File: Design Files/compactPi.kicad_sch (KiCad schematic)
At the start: 8 parts, among them J15 USB_C_Receptacle_USB2.0, U22 WE-TVS-82400102, U23 WE-TVS-82400102

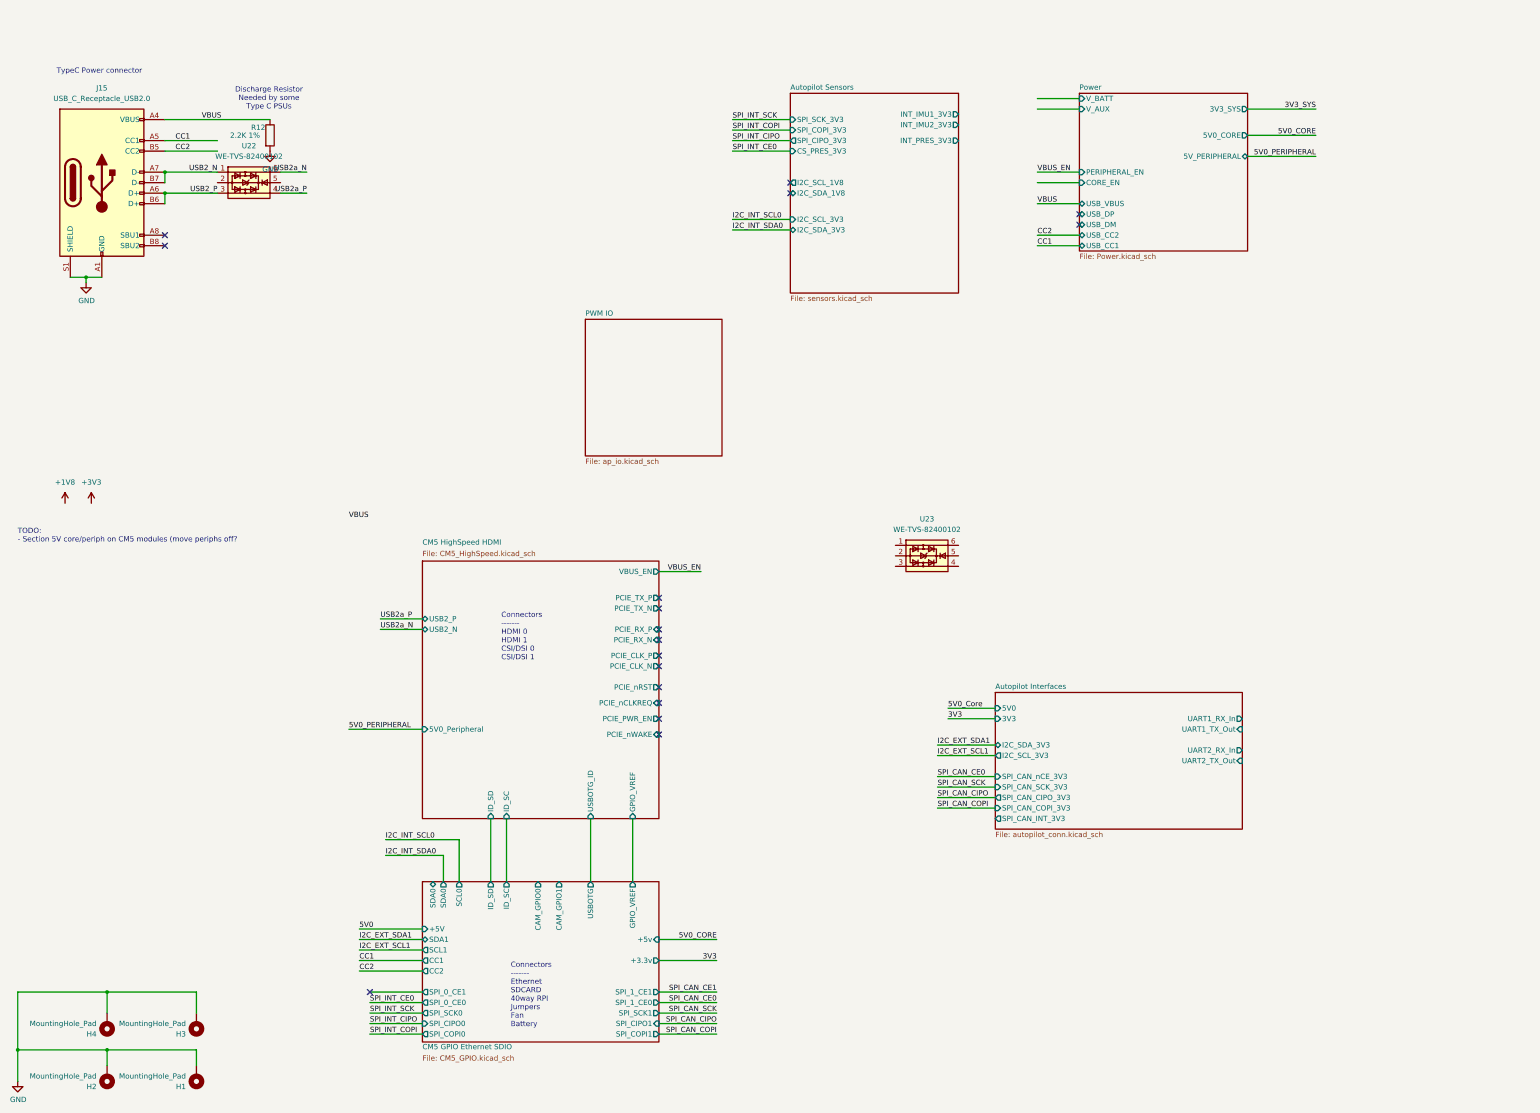
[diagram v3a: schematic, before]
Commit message: Fixed power & GPIO nets
Added PWM I2C Bus
Replaced global power labels on the sensor page with hierarchical pins & page labels
Cleaned up CM5 GPIO block sheet
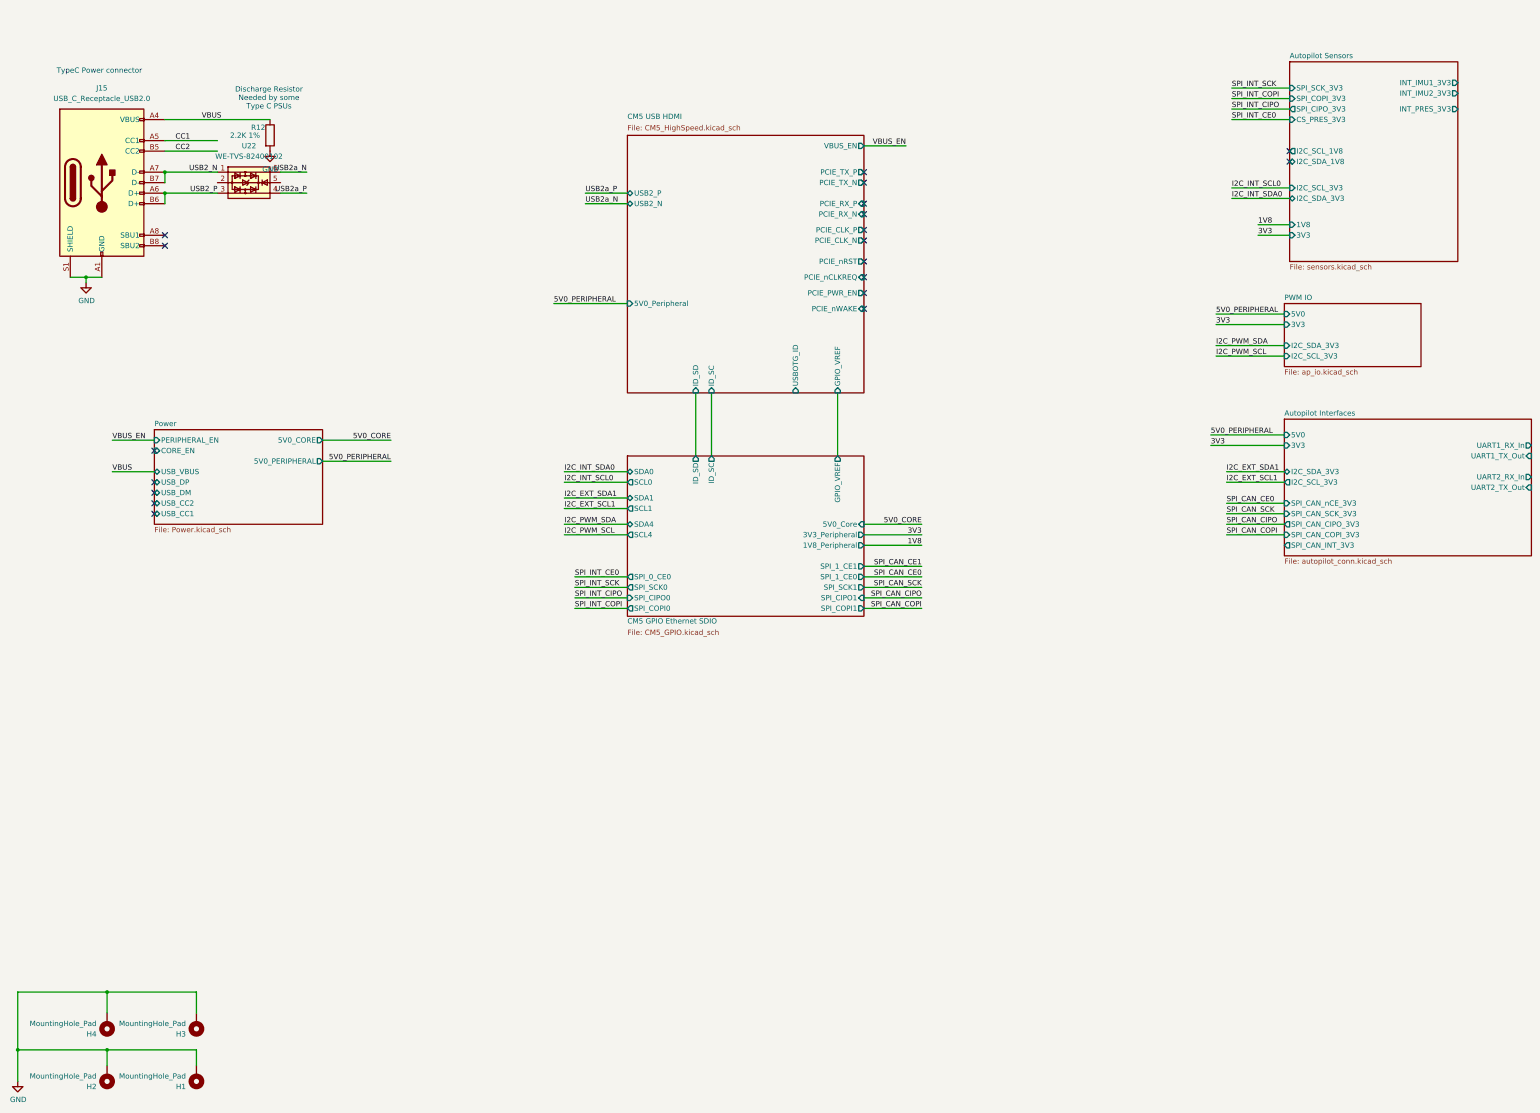
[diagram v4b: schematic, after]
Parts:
- removed U23: WE-TVS-82400102, Package_TO_SOT_SMD:SOT-23-6, symbol Power_Protection:WE-TVS-82400102
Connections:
- no-connect marks 17 -> 19
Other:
- sheet CM5 HighSpeed HDMI renamed CM5 USB HDMI
- sheet Autopilot Sensors ports: added 1V8, 3V3; removed none
- sheet CM5 GPIO Ethernet SDIO ports: added 1V8_Peripheral, 3V3_Peripheral, 5V0_Core, SCL4, SDA4; removed +3.3v, +5V, +5v, CAM_GPIO0, CAM_GPIO1, CC1, CC2, SPI_0_CE1, USBOTG
- sheet PWM IO ports: added 3V3, 5V0, I2C_SCL_3V3, I2C_SDA_3V3; removed none
- sheet Power ports: added 5V0_PERIPHERAL; removed 3V3_SYS, 5V_PERIPHERAL, V_AUX, V_BATT
- note removed: "Connectors ------- Ethernet SDCARD 40way RPI Jumpers Fan Battery"
- note removed: "Connectors ------- HDMI 0 HDMI 1 CSI/DSI 0 CSI/DSI 1"
- note removed: "TODO: - Section 5V core/periph on CM5 modules (move periphs off?"

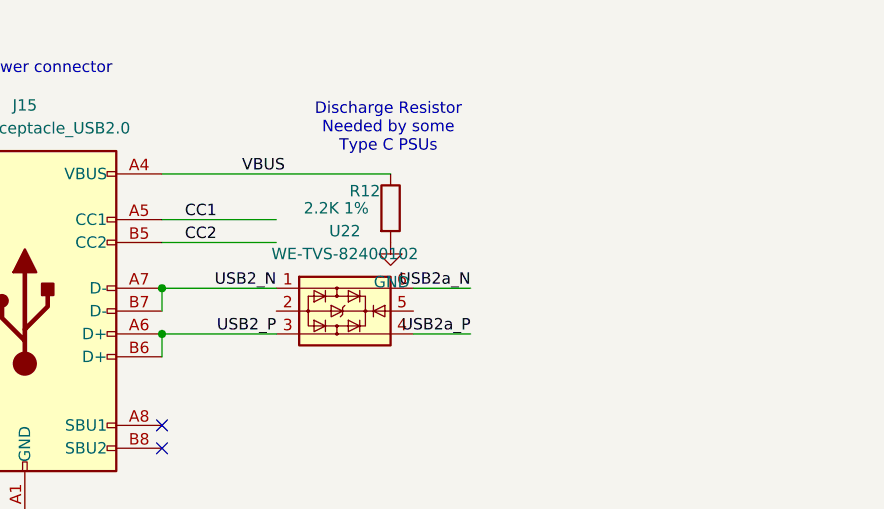
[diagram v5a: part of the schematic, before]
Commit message: SD pwr routed
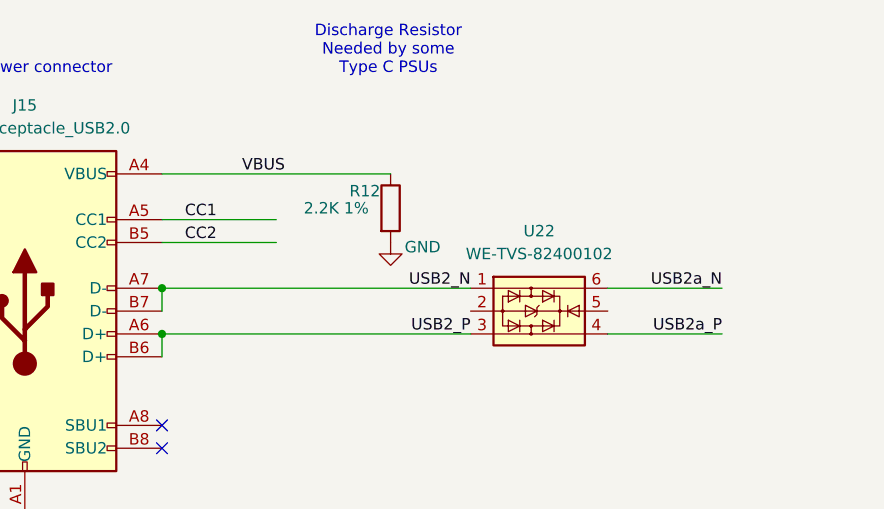
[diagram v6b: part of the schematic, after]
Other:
- moved on the sheet: U22
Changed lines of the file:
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@@
 	(text "Discharge Resistor\nNeeded by some\nType C PSUs"
 		(exclude_from_sim no)
-		(at 77.216 40.64 0)
+		(at 77.216 32.004 0)
 		(effects
 			(font
@@
 	)
 	(junction
-		(at 38.1 270.51)
+		(at 52.07 58.42)
 		(diameter 0)
 		(color 0 0 0 0)
 	)
 	(junction
-		(at 52.07 58.42)
+		(at 38.1 270.51)
 		(diameter 0)
 		(color 0 0 0 0)
@@
 	(wire
 		(pts
-			(xy 80.01 63.5) (xy 86.36 63.5)
+			(xy 101.6 63.5) (xy 114.3 63.5)
 		)
 		(stroke
@@
 	(wire
 		(pts
-			(xy 52.07 58.42) (xy 64.77 58.42)
-		)
-		(stroke
-			(width 0)
-			(type default)
-		)
-	)
-	(wire
-		(pts
 			(xy 151.13 161.29) (xy 163.83 161.29)
 		)
@@
 	(wire
 		(pts
-			(xy 52.07 63.5) (xy 64.77 63.5)
-		)
-		(stroke
-			(width 0)
-			(type default)
-		)
-	)
-	(wire
-		(pts
 			(xy 220.98 158.75) (xy 234.95 158.75)
 		)
@@
 	(wire
 		(pts
-			(xy 80.01 58.42) (xy 86.36 58.42)
+			(xy 101.6 58.42) (xy 114.3 58.42)
 		)
 		(stroke
@@
 	(wire
 		(pts
+			(xy 52.07 63.5) (xy 86.36 63.5)
+		)
+		(stroke
+			(width 0)
+			(type default)
+		)
+	)
+	(wire
+		(pts
 			(xy 309.88 45.72) (xy 323.85 45.72)
 		)
@@
 		(pts
 			(xy 308.61 130.81) (xy 322.58 130.81)
+		)
+		(stroke
+			(width 0)
+			(type default)
+		)
+	)
+	(wire
+		(pts
+			(xy 52.07 58.42) (xy 86.36 58.42)
 		)
 		(stroke
@@
 	)
 	(label "USB2a_P"
-		(at 86.36 63.5 180)
+		(at 114.3 63.5 180)
 		(effects
 			(font
@@
 	)
 	(label "USB2_P"
-		(at 64.77 63.5 180)
+		(at 86.36 63.5 180)
 		(effects
 			(font
@@
 	)
 	(label "USB2_N"
-		(at 64.77 58.42 180)
+		(at 86.36 58.42 180)
 		(effects
 			(font
@@
 	)
 	(label "USB2a_N"
-		(at 86.36 58.42 180)
+		(at 114.3 58.42 180)
 		(effects
 			(font
@@
 		)
 		(property "Value" "GND"
-			(at 77.597 57.7342 0)
+			(at 81.026 53.848 0)
 			(show_name no)
 			(do_not_autoplace no)
@@
 	(symbol
 		(lib_id "Power_Protection:WE-TVS-82400102")
-		(at 72.39 60.96 0)
+		(at 93.98 60.96 0)
 		(unit 1)
 		(body_style 1)
@@
 		(fields_autoplaced yes)
 		(property "Reference" "U22"
-			(at 72.39 52.07 0)
+			(at 93.98 52.07 0)
 			(show_name no)
 			(do_not_autoplace no)
@@
 		)
 		(property "Value" "WE-TVS-82400102"
-			(at 72.39 54.61 0)
+			(at 93.98 54.61 0)
 			(show_name no)
 			(do_not_autoplace no)
@@
 		)
 		(property "Footprint" "Package_TO_SOT_SMD:SOT-23-6"
-			(at 72.39 66.04 0)
+			(at 93.98 66.04 0)
 			(hide yes)
 			(show_name no)
@@
 		)
 		(property "Datasheet" "https://www.we-online.com/components/products/datasheet/82400102.pdf"
-			(at 72.39 67.31 0)
+			(at 93.98 67.31 0)
 			(hide yes)
 			(show_name no)
@@
 		)
 		(property "Description" "Low Capacitance TVS Diode Array, 2 Channels, SOT-23-6"
-			(at 72.39 60.96 0)
-			(hide yes)
-			(show_name no)
+			(at 93.98 60.96 0)
+			(hide yes)
+			(show_name no)
